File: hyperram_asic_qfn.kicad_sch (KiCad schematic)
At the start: 45 parts, among them IC1 W25Q32JVSSIQ_TR, IC2 S27KL0641DABHI020, IC3 LP5907UVX-1.8_NOPB, IC4 LP5907UVX-3.3_NOPB, IC5 LP5907MFX-3.3_NOPB, IC6 MCP1824T-1802E_OT, J1 USB_B_Micro, J2 Conn_02x03_Counter_Clockwise, J3 1156915, J4 1156915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

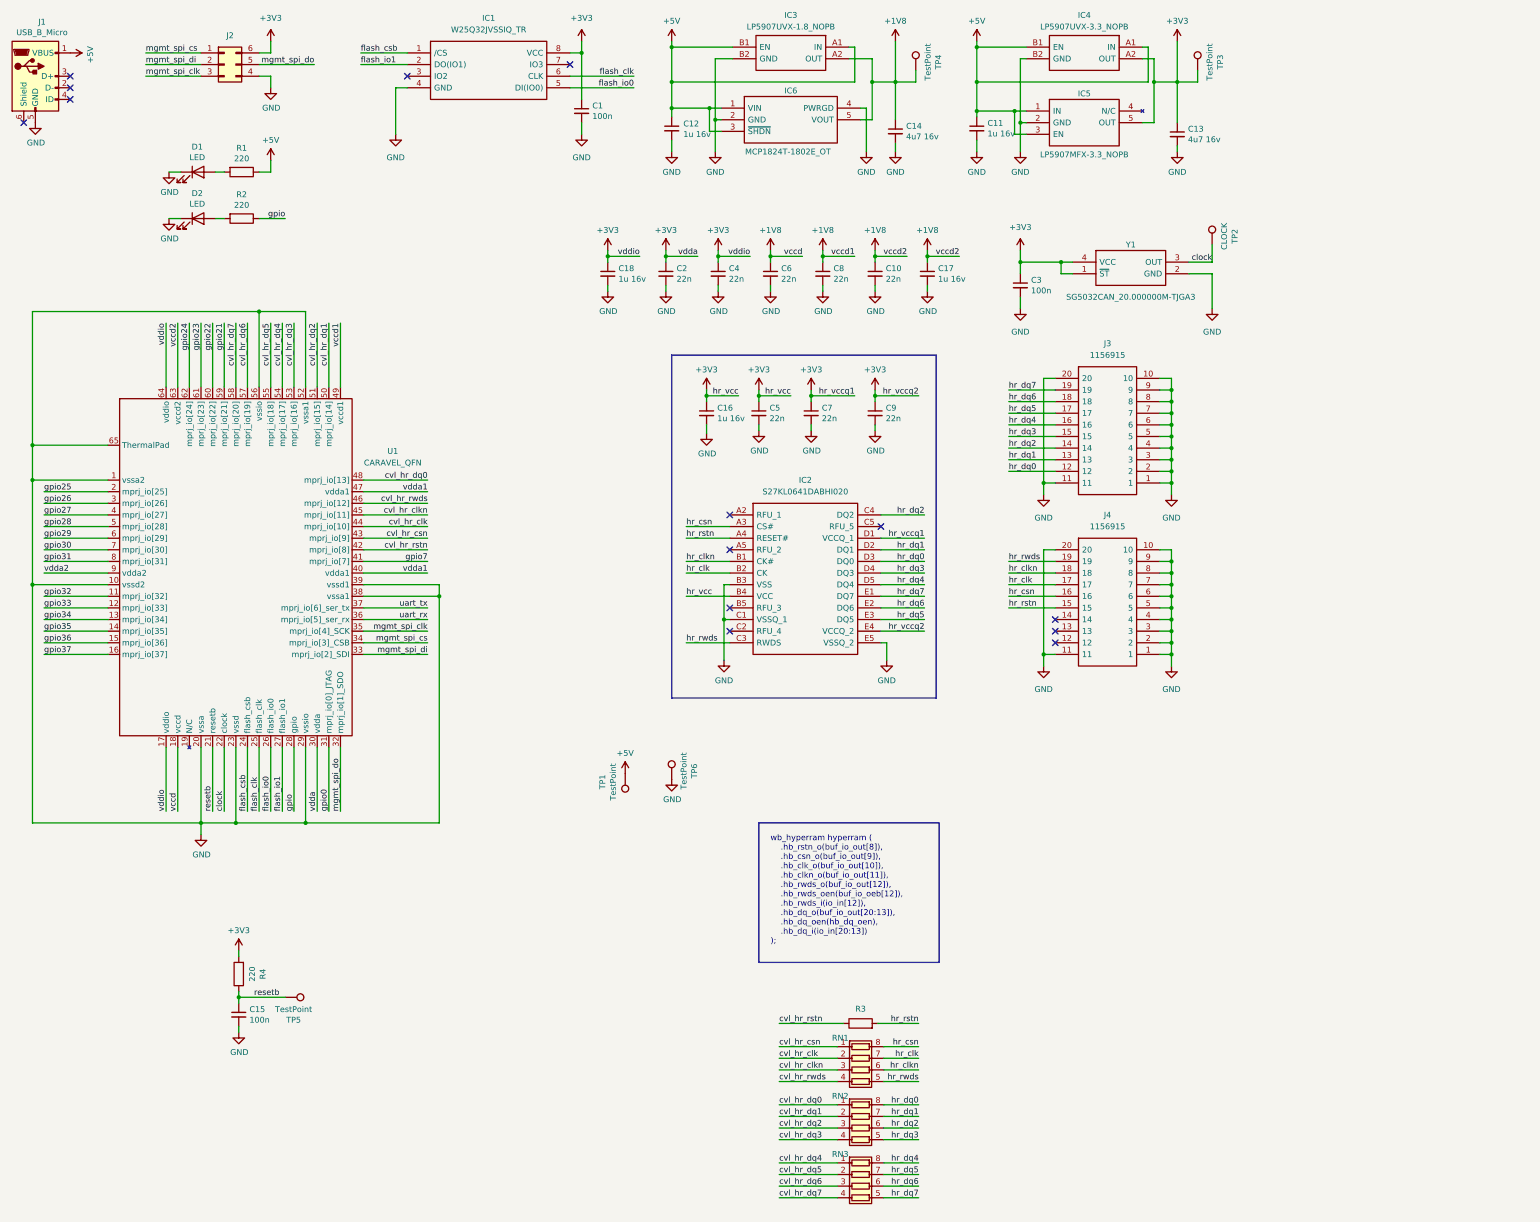
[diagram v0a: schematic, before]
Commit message: Added GPIO header. Cleaned up ERC warnings and errors in schematic.
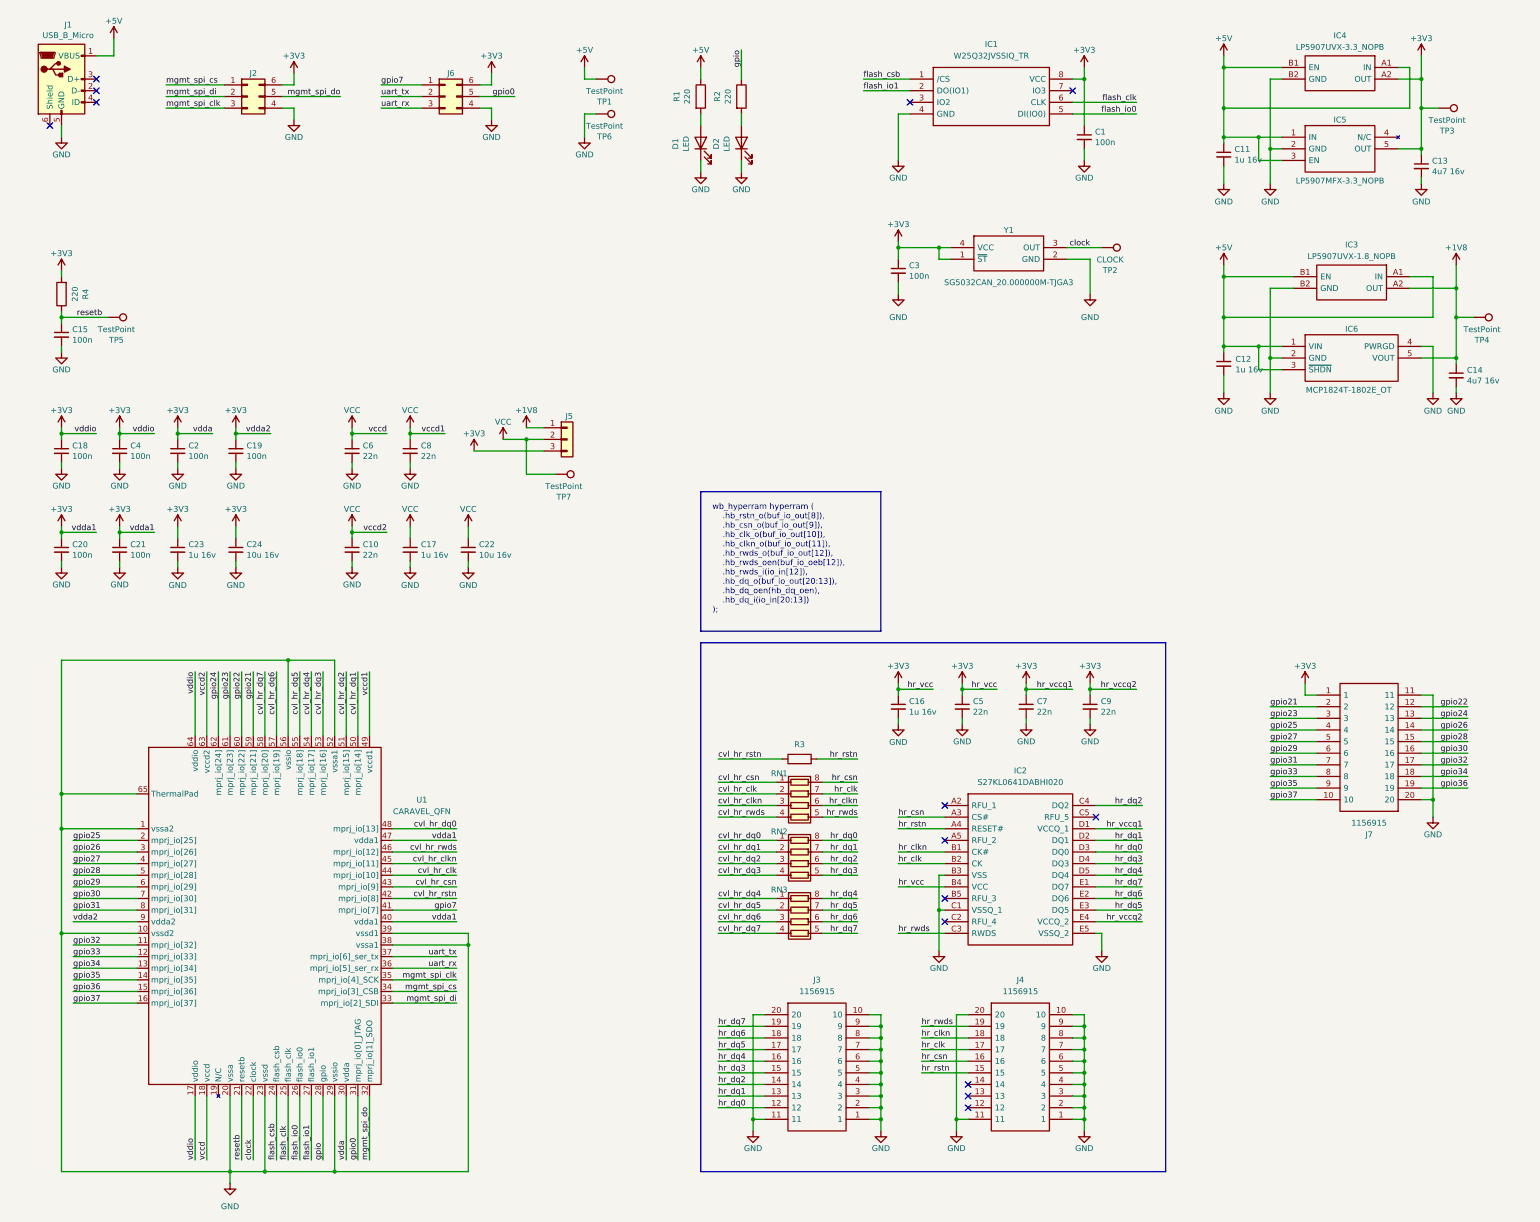
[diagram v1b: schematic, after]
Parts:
- added C19, C20, C21: 100n, Capacitor_SMD:C_0402_1005Metric_Pad0.74x0.62mm_HandSolder, symbol Device:C_Small
- added C22, C24: 10u 16v, Capacitor_SMD:C_0805_2012Metric_Pad1.18x1.45mm_HandSolder, symbol Device:C_Small
- added C23: 1u 16v, Capacitor_SMD:C_0805_2012Metric_Pad1.18x1.45mm_HandSolder, symbol Device:C_Small
- added J5: Conn_01x03, Connector_PinHeader_2.54mm:PinHeader_1x03_P2.54mm_Vertical, symbol Connector_Generic:Conn_01x03
- added J6: Conn_02x03_Counter_Clockwise, Connector_PinHeader_2.54mm:PinHeader_2x03_P2.54mm_Vertical, symbol Connector_Generic:Conn_02x03_Counter_Clockwise
- added J7: 1156915, 1156915, symbol hyperram_asic_qfn:1156915
- added TP7: TestPoint, TestPoint:TestPoint_Pad_D1.0mm, symbol Connector:TestPoint
- C18: value 1u 16v -> 100n; footprint Capacitor_SMD:C_0805_2012Metric_Pad1.18x1.45mm_HandSolder -> Capacitor_SMD:C_0402_1005Metric_Pad0.74x0.62mm_HandSolder
- C2, C4: value 22n -> 100n
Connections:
- net vdda1 is gone; now on net +3V3: U1.40 (vdda1), U1.47 (vdda1)
- net vdda2 is gone; now on net +3V3: U1.9 (vdda2)
- net +1V8: now also J5.1 (Pin_1); no longer C10.1, C17.1, C6.1, C8.1, U1.18 (vccd), U1.49 (vccd1), U1.63 (vccd2)
- net +3V3: now also C19.1, C20.1, C21.1, C23.1, C24.1, J5.3 (Pin_3), J6.6 (Pin_6), J7.1
- net GND: now also C19.2, C20.2, C21.2, C22.2, C23.2, C24.2, J6.4 (Pin_4), J7.11, J7.20
- net gpio0: now also J6.5 (Pin_5)
- net gpio21: now also J7.2
- net gpio22: now also J7.12
- net gpio23: now also J7.3
- net gpio24: now also J7.13
- net gpio25: now also J7.4
- net gpio26: now also J7.14
- net gpio27: now also J7.5
- net gpio28: now also J7.15
- net gpio29: now also J7.6
- net gpio30: now also J7.16
- net gpio31: now also J7.7
- net gpio32: now also J7.17
- net gpio33: now also J7.8
- net gpio34: now also J7.18
- net gpio35: now also J7.9
- net gpio36: now also J7.19
- net gpio37: now also J7.10
- net gpio7: now also J6.1 (Pin_1)
- net uart_rx: now also J6.3 (Pin_3)
- net uart_tx: now also J6.2 (Pin_2)
- new net VCC: C10.1, C17.1, C22.1, C6.1, C8.1, J5.2 (Pin_2), TP7.1, U1.18 (vccd), U1.49 (vccd1), U1.63 (vccd2)
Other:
- moved on the sheet: C1, C10, C11, C12, C13, C14, C15, C16, C17, C18, C2, C3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

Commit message: Updated schematic: resistors instead of jumpers to select VCC, integrated two smaller headers into one bigger.
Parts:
- removed J2, J6: Conn_02x03_Counter_Clockwise, Connector_PinHeader_2.54mm:PinHeader_2x03_P2.54mm_Vertical, symbol Connector_Generic:Conn_02x03_Counter_Clockwise
- removed J5: Conn_01x03, Connector_PinHeader_2.54mm:PinHeader_1x03_P2.54mm_Vertical, symbol Connector_Generic:Conn_01x03
- added J2: Conn_02x06_Odd_Even, Connector_PinHeader_2.54mm:PinHeader_2x06_P2.54mm_Vertical, symbol Connector_Generic:Conn_02x06_Odd_Even
- added R5: 0, Resistor_SMD:R_0603_1608Metric, symbol Device:R
- added R6: NC, Resistor_SMD:R_0603_1608Metric, symbol Device:R
- C10, C5, C6, C7, C8, C9: value 22n -> 100n
- R4: value 220 -> 2k2
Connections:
- net +1V8: now also R5.2
- net +3V3: now also J2.10 (Pin_10), J2.9 (Pin_9), R6.2
- net GND: now also J2.11 (Pin_11), J2.12 (Pin_12)
- net VCC: now also R5.1, R6.1
- net gpio0: now also J2.7 (Pin_7)
- net gpio7: now also J2.8 (Pin_8)
- net mgmt_spi_clk: now also J2.4 (Pin_4)
- net mgmt_spi_cs: now also J2.3 (Pin_3)
- net mgmt_spi_di: now also J2.2 (Pin_2)
- net mgmt_spi_do: now also J2.1 (Pin_1)
- net uart_rx: now also J2.5 (Pin_5)
- net uart_tx: now also J2.6 (Pin_6)
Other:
- note added: "MPW-8 -> R5 populated only, GFMPW-0 -> R6 populated only"
- moved on the sheet: TP7

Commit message: Fixed package assignments and library. Reordered signals to easy routing pcb.
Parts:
- removed J7: 1156915, 1156915, symbol hyperram_asic_qfn:1156915
- added J7: Conn_02x10_Odd_Even, Connector_PinHeader_2.54mm:PinHeader_2x10_P2.54mm_Vertical, symbol Connector_Generic:Conn_02x10_Odd_Even
- C22, C24: value 10u 16v -> 22u 25v
- IC1: footprint SOIC127P790X216-8N -> hyperram_asic_qfn:SOIC127P790X216-8N
- IC2: footprint BGA24C100P5X5_600X800X100 -> hyperram_asic_qfn:BGA24C100P5X5_600X800X100
- IC3: footprint BGA4C35P2X2_64X64X44 -> hyperram_asic_qfn:BGA4C35P2X2_64X64X44
- IC4: footprint BGA4C35P2X2_64X64X33 -> hyperram_asic_qfn:BGA4C35P2X2_64X64X33
- J3, J4: footprint 1156915 -> hyperram_asic_qfn:1156915
- Y1: footprint SG5032CAN20000000MTJGA3 -> hyperram_asic_qfn:SG5032CAN20000000MTJGA3
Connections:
- net +3V3: now also J2.1 (Pin_1), J2.2 (Pin_2), J7.1 (Pin_1); no longer J2.10 (Pin_10), J2.9 (Pin_9)
- net GND: now also J2.3 (Pin_3), J2.4 (Pin_4), J7.2 (Pin_2), J7.20 (Pin_20); no longer J2.11 (Pin_11), J2.12 (Pin_12)
- net cvl_hr_clk: now also RN1.3 (R3.1); no longer RN1.2 (R2.1)
- net cvl_hr_clkn: now also RN1.2 (R2.1); no longer RN1.3 (R3.1)
- net cvl_hr_csn: now also RN1.4 (R4.1); no longer RN1.1 (R1.1)
- net cvl_hr_dq0: now also RN2.4 (R4.1); no longer RN2.1 (R1.1)
- net cvl_hr_dq1: now also RN2.3 (R3.1); no longer RN2.2 (R2.1)
- net cvl_hr_dq2: now also RN2.2 (R2.1); no longer RN2.3 (R3.1)
- net cvl_hr_dq3: now also RN2.1 (R1.1); no longer RN2.4 (R4.1)
- net cvl_hr_dq4: now also RN3.4 (R4.1); no longer RN3.1 (R1.1)
- net cvl_hr_dq5: now also RN3.3 (R3.1); no longer RN3.2 (R2.1)
- net cvl_hr_dq6: now also RN3.2 (R2.1); no longer RN3.3 (R3.1)
- net cvl_hr_dq7: now also RN3.1 (R1.1); no longer RN3.4 (R4.1)
- net cvl_hr_rwds: now also RN1.1 (R1.1); no longer RN1.4 (R4.1)
- net gpio0: now also J2.11 (Pin_11); no longer J2.7 (Pin_7)
- net gpio21: now also J7.3 (Pin_3)
- net gpio22: now also J7.4 (Pin_4)
- net gpio23: now also J7.5 (Pin_5)
- net gpio24: now also J7.6 (Pin_6)
- net gpio25: now also J7.7 (Pin_7)
- net gpio26: now also J7.8 (Pin_8)
- net gpio27: now also J7.9 (Pin_9)
- net gpio28: now also J7.10 (Pin_10)
- net gpio29: now also J7.11 (Pin_11)
- net gpio30: now also J7.12 (Pin_12)
- net gpio31: now also J7.13 (Pin_13)
- net gpio32: now also J7.14 (Pin_14)
- net gpio33: now also J7.15 (Pin_15)
- net gpio34: now also J7.16 (Pin_16)
- net gpio35: now also J7.17 (Pin_17)
- net gpio36: now also J7.18 (Pin_18)
- net gpio37: now also J7.19 (Pin_19)
- net gpio7: now also J2.12 (Pin_12); no longer J2.8 (Pin_8)
- net hr_clk: now also RN1.6 (R3.2); no longer RN1.7 (R2.2)
- net hr_clkn: now also RN1.7 (R2.2); no longer RN1.6 (R3.2)
- net hr_csn: now also RN1.5 (R4.2); no longer RN1.8 (R1.2)
- net hr_dq0: now also RN2.5 (R4.2); no longer RN2.8 (R1.2)
- net hr_dq1: now also RN2.6 (R3.2); no longer RN2.7 (R2.2)
- net hr_dq2: now also RN2.7 (R2.2); no longer RN2.6 (R3.2)
- net hr_dq3: now also RN2.8 (R1.2); no longer RN2.5 (R4.2)
- net hr_dq4: now also RN3.5 (R4.2); no longer RN3.8 (R1.2)
- net hr_dq5: now also RN3.6 (R3.2); no longer RN3.7 (R2.2)
- net hr_dq6: now also RN3.7 (R2.2); no longer RN3.6 (R3.2)
- net hr_dq7: now also RN3.8 (R1.2); no longer RN3.5 (R4.2)
- net hr_rwds: now also RN1.8 (R1.2); no longer RN1.5 (R4.2)
- net mgmt_spi_clk: now also J2.8 (Pin_8); no longer J2.4 (Pin_4)
- net mgmt_spi_cs: now also J2.7 (Pin_7); no longer J2.3 (Pin_3)
- net mgmt_spi_di: now also J2.6 (Pin_6); no longer J2.2 (Pin_2)
- net mgmt_spi_do: now also J2.5 (Pin_5); no longer J2.1 (Pin_1)
- net uart_rx: now also J2.9 (Pin_9); no longer J2.5 (Pin_5)
- net uart_tx: now also J2.10 (Pin_10); no longer J2.6 (Pin_6)

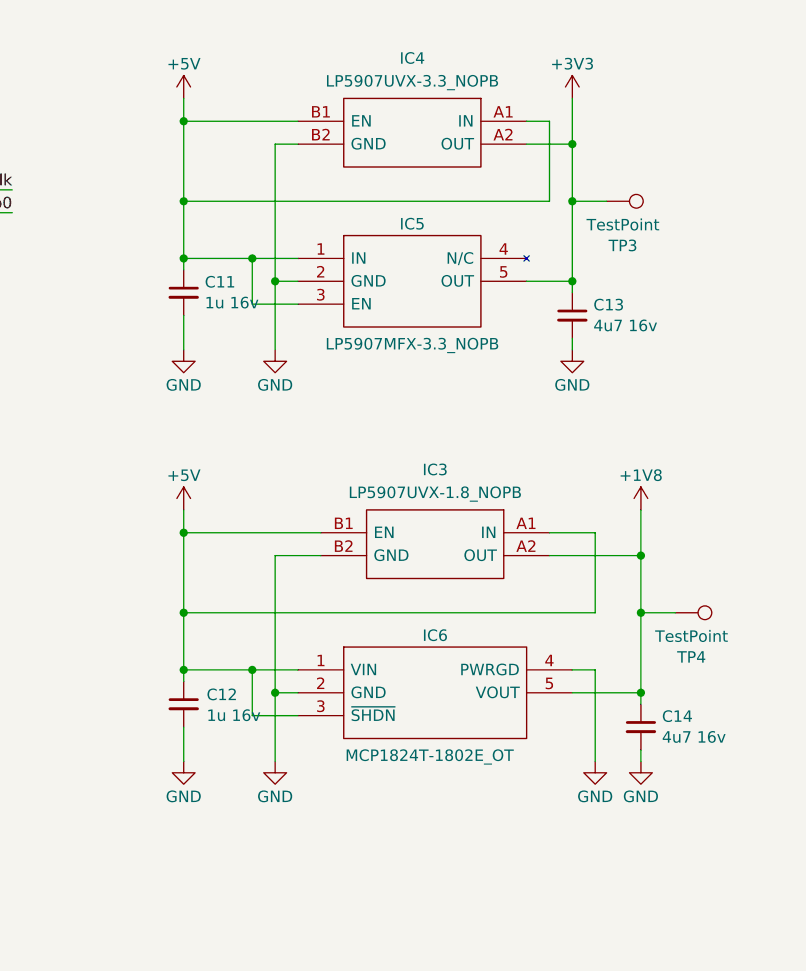
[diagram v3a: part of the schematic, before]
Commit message: Removed duplicated LDOs in BGA packages.
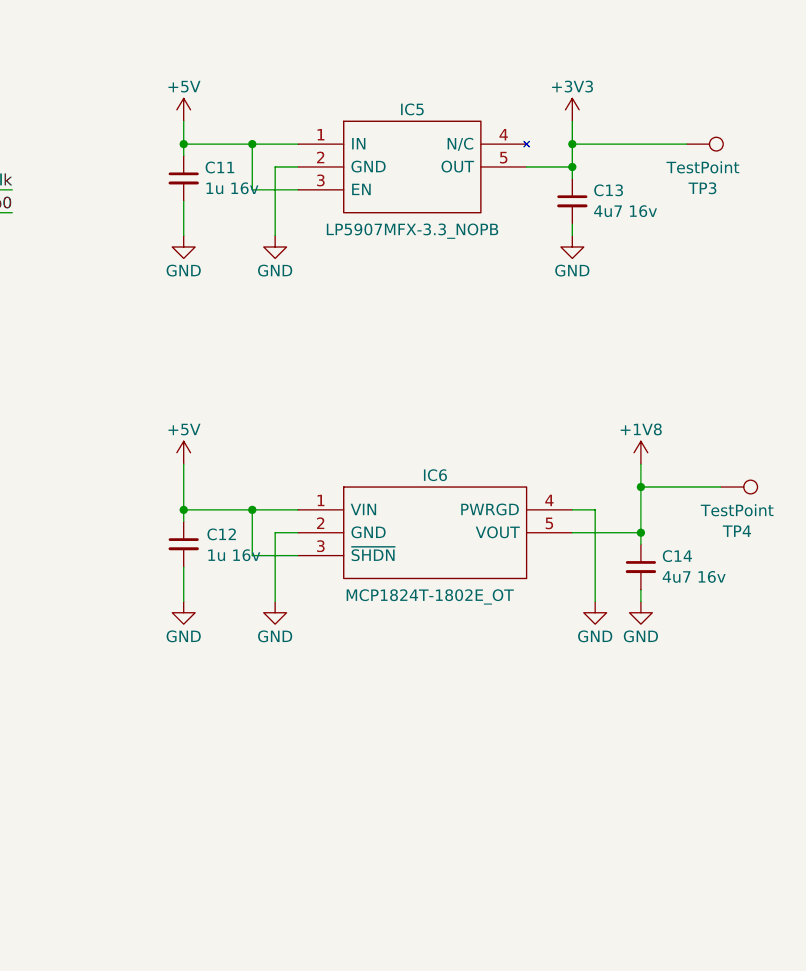
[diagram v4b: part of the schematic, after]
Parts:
- removed IC3: LP5907UVX-1.8_NOPB, hyperram_asic_qfn:BGA4C35P2X2_64X64X44, symbol hyperram_asic_qfn:LP5907UVX-1.8_NOPB
- removed IC4: LP5907UVX-3.3_NOPB, hyperram_asic_qfn:BGA4C35P2X2_64X64X33, symbol hyperram_asic_qfn:LP5907UVX-3.3_NOPB
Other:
- moved on the sheet: C11, C12, C13, C14, IC5, IC6, TP3, TP4

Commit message: Updated Testpoints description to voltage values.
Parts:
- TP1: value TestPoint -> 5V
- TP2: value CLOCK -> CLK
- TP3: value TestPoint -> 3V3
- TP4: value TestPoint -> 1V8
- TP6: value TestPoint -> GND
- TP7: value TestPoint -> VCC
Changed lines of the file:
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@@
 			)
 		)
-		(property "Value" "TestPoint"
+		(property "Value" "1V8"
 			(at 340.9188 68.6816 90)
 			(effects
@@
 			)
 		)
-		(property "Value" "TestPoint"
+		(property "Value" "3V3"
 			(at 337.1088 30.5816 90)
 			(effects
@@
 			)
 		)
-		(property "Value" "TestPoint"
+		(property "Value" "VCC"
 			(at 112.3188 82.6516 90)
 			(effects
@@
 			)
 		)
-		(property "Value" "CLOCK"
+		(property "Value" "CLK"
 			(at 254.5588 67.4116 90)
 			(effects
@@
 			)
 		)
-		(property "Value" "TestPoint"
+		(property "Value" "GND"
 			(at 144.0688 38.2016 90)
 			(effects
@@
 			)
 		)
-		(property "Value" "TestPoint"
+		(property "Value" "5V"
 			(at 144.0688 30.5816 90)
 			(effects

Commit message: Added missing resistance value for R3
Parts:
- R3: value R -> 22
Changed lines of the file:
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@@
 			)
 		)
-		(property "Value" "R"
+		(property "Value" "22"
 			(at 186.69 173.355 90)
 			(effects
